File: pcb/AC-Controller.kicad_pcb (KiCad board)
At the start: 2 copper layers, 66 x 67 mm, 84 parts, among them J1 Serial, J2 USB_C_Top, J3 USB_C_Bottom, Q1 AO3400A, Q2 AO3401A, Q3 AO3400A, Q4 BSS84, Q5 BSS84, Q6 BSS84, Q7 BSS84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

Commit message: feat: add power switch
Add switch to disconnect battery power from the circuit for when the device is not in use for a long time and reduce power consumption to a few nA
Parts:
- added D4: 1N4148WS, Diode_SMD:D_SOD-323, F.Cu at (177.5, 99.5)
- added Q8: AO3400A, Package_TO_SOT_SMD:SOT-23, F.Cu at (165.0, 87.8)
- added R34: 100k, Resistor_SMD:R_0402_1005Metric, F.Cu at (177.5, 96.5)
- added SW4: Power, Button_Switch_SMD:SW_SPDT_PCM12, F.Cu at (181.0, 98.8)
- moved Q3 0.56 mm to (168.5, 87.8), turned to -90 degrees
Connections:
- Q3 pad 1: /Battery+ -> /Power/B_{gate}
- Q3 pad 2: GND -> /Power/Bp
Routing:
- net /Power/B_{gate}: track 0.00 -> 26.6 mm, vias 0 -> 3
- net /Power/B-: track 3.42 -> 15.1 mm, vias 0 -> 1
- net /Battery+: track 84.8 -> 95.4 mm, vias 2 -> 3
- net /Power/Bp: track 0.00 -> 2.75 mm
- net Net-(SW4-C): track 0.00 -> 1.81 mm
- net /LCD_BL: track 91.1 -> 90.4 mm

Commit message: style: cleanup
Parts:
- renumbered Q8 to Q4, Q4 to Q5, Q5 to Q6, Q6 to Q7, Q7 to Q8
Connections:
- net Net-(SW4-C) renamed /Power/B_{dis}
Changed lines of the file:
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@@
   (net 62 "/LCD_K")
   (net 63 "/WakeUp")
-  (net 64 "Net-(SW4-C)")
+  (net 64 "/Power/B_{dis}")
   (net 65 "/Power/Bp")
   (net 66 "/Power/B_{gate}")
@@
     (property "ki_keywords" "P-Channel MOSFET")
     (attr smd)
-    (fp_text reference "Q2" (at -1.5 0 180) (layer "F.SilkS")
+    (fp_text reference "Q2" (at 1.5 -1 180) (layer "F.SilkS")
         (effects (font (size 0.8 0.8) (thickness 0.15)))
     )
@@
     (property "ki_keywords" "P-Channel MOSFET")
     (attr smd)
-    (fp_text reference "Q7" (at -1.45 0) (layer "F.SilkS")
+    (fp_text reference "Q8" (at 1.5 -1) (layer "F.SilkS")
         (effects (font (size 0.8 0.8) (thickness 0.15)))
     )
@@
     (property "ki_keywords" "P-Channel MOSFET")
     (attr smd)
-    (fp_text reference "Q5" (at -1.45 0) (layer "F.SilkS")
+    (fp_text reference "Q6" (at 1.5 -1) (layer "F.SilkS")
         (effects (font (size 0.8 0.8) (thickness 0.15)))
     )
@@
     (property "ki_keywords" "N-Channel MOSFET")
     (attr smd)
-    (fp_text reference "Q3" (at -1.5 0 90) (layer "F.SilkS")
+    (fp_text reference "Q3" (at 1.25 -1.25 -180) (layer "F.SilkS")
         (effects (font (size 0.8 0.8) (thickness 0.15)))
     )
@@
     (property "ki_keywords" "P-Channel MOSFET")
     (attr smd)
-    (fp_text reference "Q6" (at -1.45 0) (layer "F.SilkS")
+    (fp_text reference "Q7" (at 1.5 -1) (layer "F.SilkS")
         (effects (font (size 0.8 0.8) (thickness 0.15)))
     )
@@
       (net 66 "/Power/B_{gate}") (pinfunction "B") (pintype "passive"))
     (pad "3" smd rect (at 2.25 -1.43 90) (size 0.7 1.5) (layers "F.Cu" "F.Paste" "F.Mask")
-      (net 64 "Net-(SW4-C)") (pinfunction "C") (pintype "passive"))
+      (net 64 "/Power/B_{dis}") (pinfunction "C") (pintype "passive"))
     (model "${KICAD6_3DMODEL_DIR}/Button_Switch_SMD.3dshapes/SW_SPDT_PCM12.wrl"
       (offset (xyz 0 0 0))
@@
     (property "ki_keywords" "N-Channel MOSFET")
     (attr smd)
-    (fp_text reference "Q8" (at -1.5 0 90) (layer "F.SilkS")
+    (fp_text reference "Q4" (at 1.25 -1.25 180) (layer "F.SilkS")
         (effects (font (size 0.8 0.8) (thickness 0.15)))
     )
@@
     (property "ki_keywords" "P-Channel MOSFET")
     (attr smd)
-    (fp_text reference "Q4" (at -1.45 0) (layer "F.SilkS")
+    (fp_text reference "Q5" (at 1.5 -1) (layer "F.SilkS")
         (effects (font (size 0.8 0.8) (thickness 0.15)))
     )
@@
       (net 58 "/Power/B-") (pintype "passive"))
     (pad "2" smd roundrect (at 0.51 0) (size 0.54 0.64) (layers "F.Cu" "F.Paste" "F.Mask") (roundrect_rratio 0.25)
-      (net 64 "Net-(SW4-C)") (pintype "passive"))
+      (net 64 "/Power/B_{dis}") (pintype "passive"))
     (model "${KICAD6_3DMODEL_DIR}/Resistor_SMD.3dshapes/R_0402_1005Metric.wrl"
       (offset (xyz 0 0 0))

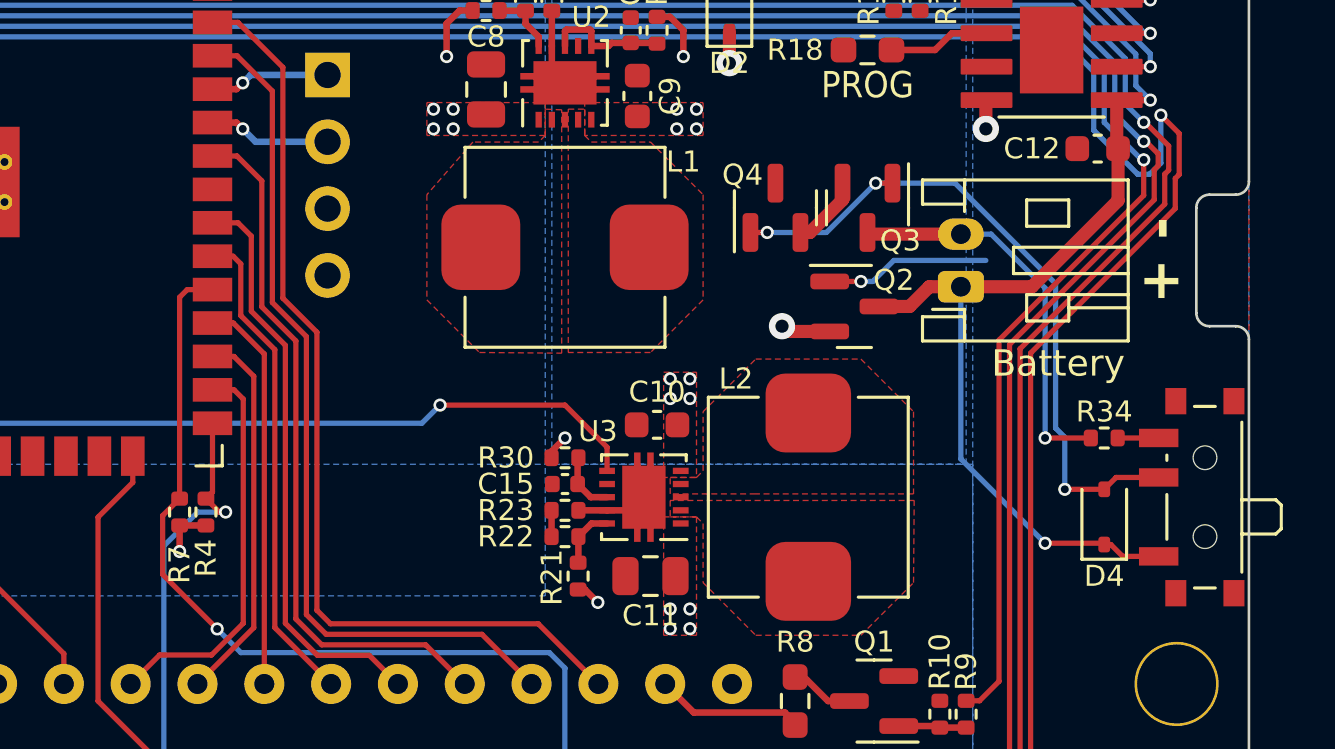
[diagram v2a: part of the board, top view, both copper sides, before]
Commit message: fix: add missing part numbers
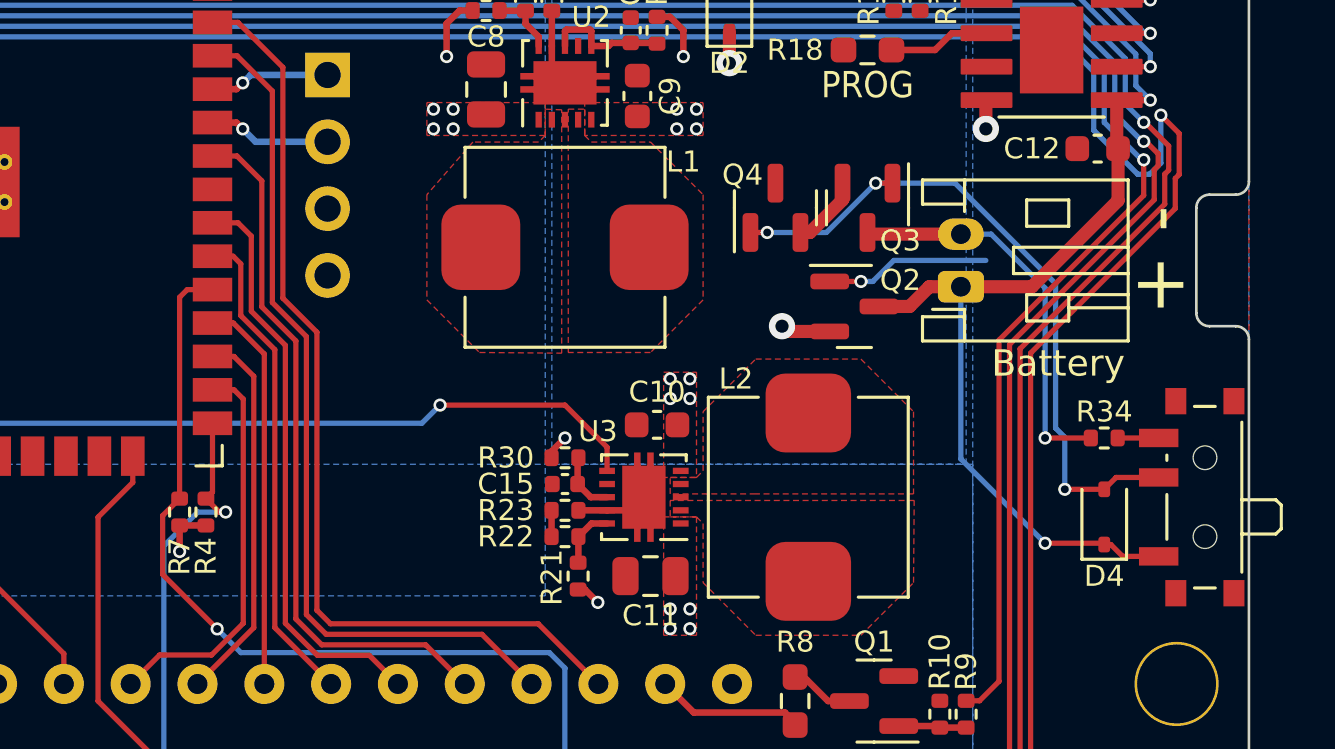
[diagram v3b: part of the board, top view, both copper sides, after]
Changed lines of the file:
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@@
     (property "ki_keywords" "P-Channel MOSFET")
     (attr smd)
-    (fp_text reference "Q2" (at 1.5 -1 180) (layer "F.SilkS")
+    (fp_text reference "Q2" (at 1.75 -1 180) (layer "F.SilkS")
         (effects (font (size 0.8 0.8) (thickness 0.15)))
     )
@@
     (descr "SOT, 3 Pin (https://www.jedec.org/system/files/docs/to-236h.pdf variant AB), generated with kicad-footprint-generator ipc_gullwing_generator.py")
     (tags "SOT TO_SOT_SMD")
+    (property "LCSC" "C8492")
     (property "Sheetfile" "AC-Controller.kicad_sch")
     (property "Sheetname" "")
@@
     (descr "SOT, 3 Pin (https://www.jedec.org/system/files/docs/to-236h.pdf variant AB), generated with kicad-footprint-generator ipc_gullwing_generator.py")
     (tags "SOT TO_SOT_SMD")
+    (property "LCSC" "C8492")
     (property "Sheetfile" "AC-Controller.kicad_sch")
     (property "Sheetname" "")
@@
     (descr "SOT, 3 Pin (https://www.jedec.org/system/files/docs/to-236h.pdf variant AB), generated with kicad-footprint-generator ipc_gullwing_generator.py")
     (tags "SOT TO_SOT_SMD")
+    (property "LCSC" "C8492")
     (property "Sheetfile" "AC-Controller.kicad_sch")
     (property "Sheetname" "")
@@
     (at 181 98.75 90)
     (descr "Ultraminiature Surface Mount Slide Switch, right-angle, https://www.ckswitches.com/media/1424/pcm.pdf")
+    (property "LCSC" "C221841")
     (property "Sheetfile" "power.kicad_sch")
     (property "Sheetname" "Power")
@@
     (property "ki_keywords" "R resistor")
     (attr smd)
-    (fp_text reference "R7" (at -2 0 90) (layer "F.SilkS")
+    (fp_text reference "R7" (at -1.685 0 90) (layer "F.SilkS")
         (effects (font (size 0.8 0.8) (thickness 0.15)))
     )
@@
     (property "ki_keywords" "R resistor")
     (attr smd)
-    (fp_text reference "R4" (at -1.75 0 90) (layer "F.SilkS")
+    (fp_text reference "R4" (at -1.685 0 90) (layer "F.SilkS")
         (effects (font (size 0.8 0.8) (thickness 0.15)))
     )
@@
     (descr "SOD-323")
     (tags "SOD-323")
+    (property "LCSC" "C2128")
     (property "Sheetfile" "power.kicad_sch")
     (property "Sheetname" "Power")
@@
     (descr "SOT, 3 Pin (https://www.jedec.org/system/files/docs/to-236h.pdf variant AB), generated with kicad-footprint-generator ipc_gullwing_generator.py")
     (tags "SOT TO_SOT_SMD")
+    (property "LCSC" "C8492")
     (property "Sheetfile" "AC-Controller.kicad_sch")
     (property "Sheetname" "")
@@
     (effects (font (size 1 1) (thickness 0.15)) (justify bottom))
   )
-  (gr_text "+ -" (at 180.5 89.75 90) (layer "F.SilkS")
-    (effects (font (size 1.5 1.5) (thickness 0.25) bold) (justify bottom))
+  (gr_text "+ -" (at 180.75 89.75 90) (layer "F.SilkS")
+    (effects (font (size 2 2) (thickness 0.3)) (justify bottom))
   )
   (gr_text "IO0" (at 142.5 116.25 90) (layer "F.SilkS")
